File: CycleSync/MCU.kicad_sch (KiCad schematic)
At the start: 0 parts

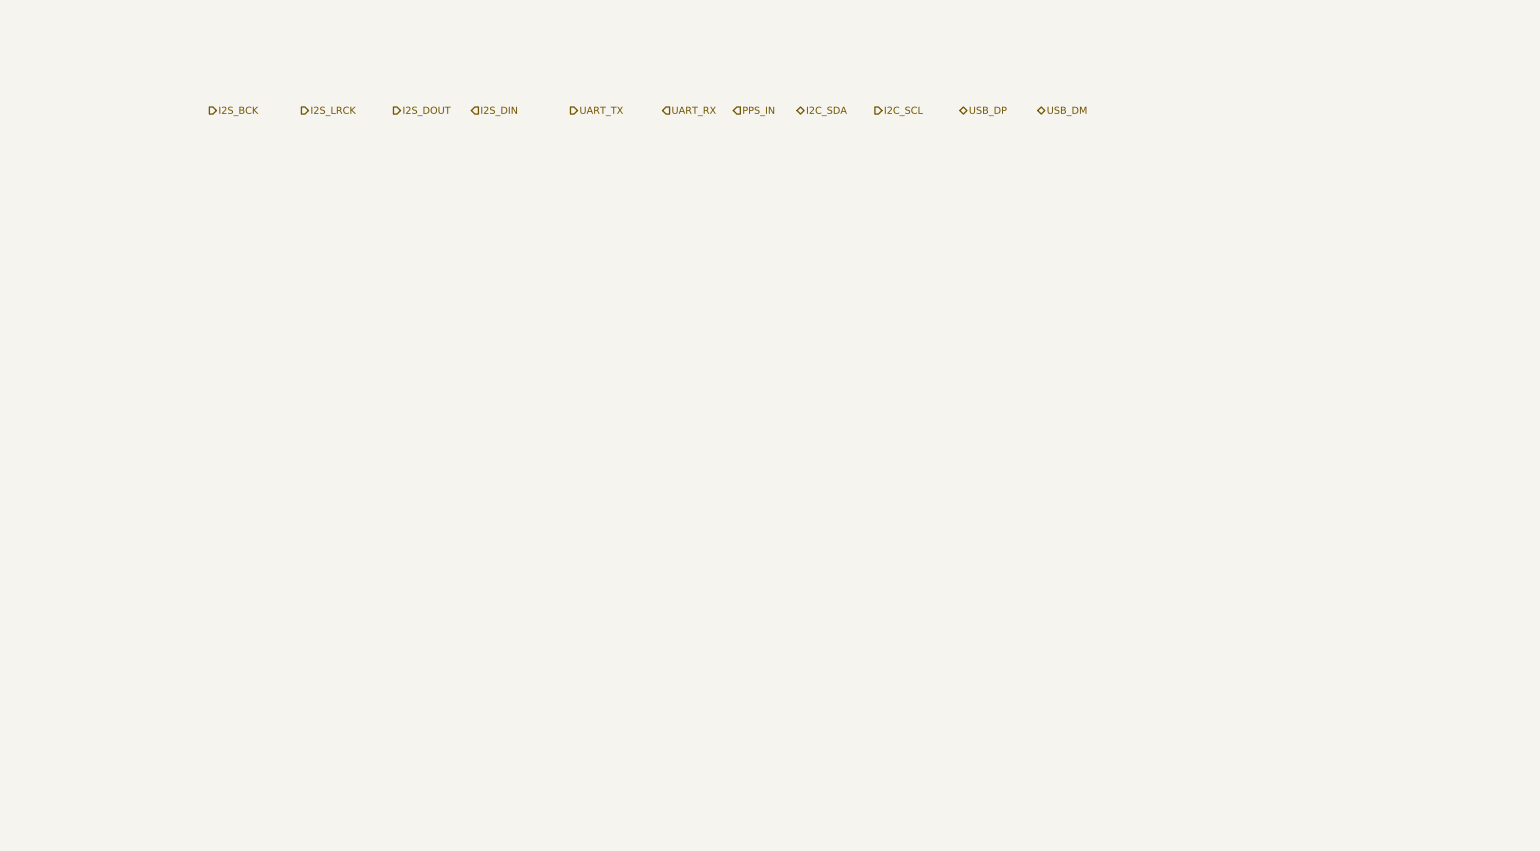
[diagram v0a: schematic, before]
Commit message: M1.2: MCU core supply, fixed-function pins, GPIO0-8 assignment
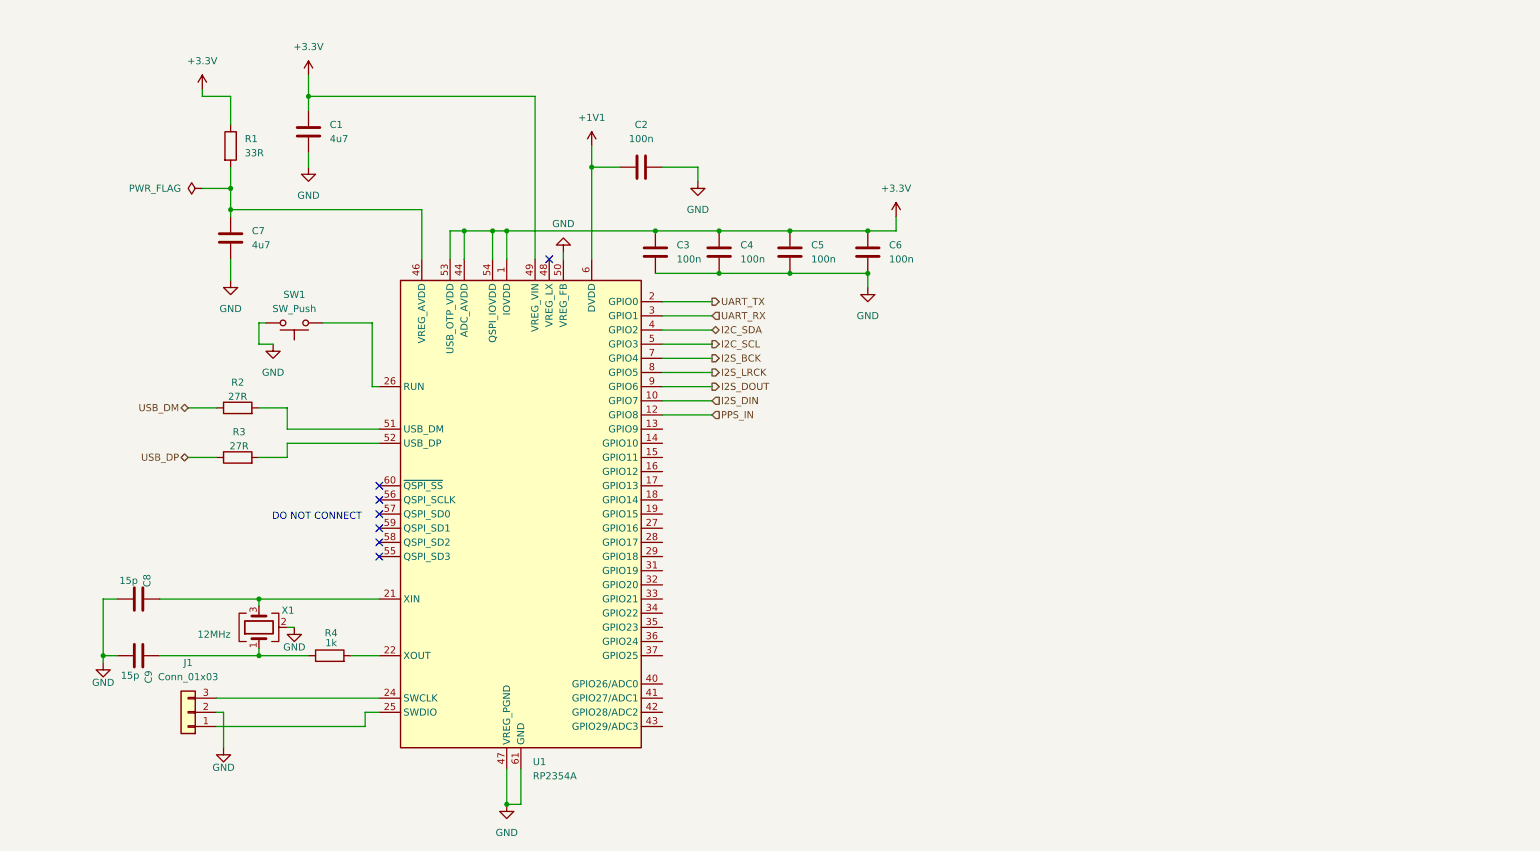
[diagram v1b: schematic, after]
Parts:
- added C1, C7: 4u7, symbol Device:C
- added C2, C3, C4, C5, C6: 100n, symbol Device:C
- added C8, C9: 15p, symbol Device:C
- added J1: Conn_01x03, symbol Connector_Generic:Conn_01x03
- added R1: 33R, symbol Device:R
- added R2, R3: 27R, symbol Device:R
- added R4: 1k, symbol Device:R
- added SW1: SW_Push, symbol Switch:SW_Push
- added U1: RP2354A, Package_DFN_QFN:QFN-60-1EP_7x7mm_P0.4mm_EP3.4x3.4mm, symbol MCU_RaspberryPi:RP2354A
- added X1: 12MHz, symbol Device:Crystal_GND24
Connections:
- net I2C_SCL: now also U1.5 (GPIO3)
- net I2C_SDA: now also U1.4 (GPIO2)
- net I2S_BCK: now also U1.7 (GPIO4)
- net I2S_DIN: now also U1.10 (GPIO7)
- net I2S_DOUT: now also U1.9 (GPIO6)
- net I2S_LRCK: now also U1.8 (GPIO5)
- net PPS_IN: now also U1.12 (GPIO8)
- net UART_RX: now also U1.3 (GPIO1)
- net UART_TX: now also U1.2 (GPIO0)
- net USB_DM: now also R2.1
- net USB_DP: now also R3.1
- new net: C9.2, R4.1, X1.1
- new net: C8.2, U1.21 (XIN), X1.3
- new net: J1.1 (Pin_1), U1.25 (SWDIO)
- new net: J1.3 (Pin_3), U1.24 (SWCLK)
- new net: R4.2, U1.22 (XOUT)
- new net: SW1.1, U1.26 (RUN)
- new net: C7.1, R1.2, U1.46 (VREG_AVDD)
- new net: R2.2, U1.51 (USB_DM)
- new net: R3.2, U1.52 (USB_DP)
- new net +1V1: C2.1, U1.23 (DVDD), U1.39 (DVDD), U1.6 (DVDD)
- new net +3.3V: C1.1, C3.2, C4.2, C5.2, C6.2, R1.1, U1.1 (IOVDD), U1.11 (IOVDD), U1.20 (IOVDD), U1.30 (IOVDD), U1.38 (IOVDD), U1.44 (ADC_AVDD), U1.45 (IOVDD), U1.49 (VREG_VIN), U1.53 (USB_OTP_VDD), U1.54 (QSPI_IOVDD)
- new net GND: C1.2, C2.2, C3.1, C4.1, C5.1, C6.1, C7.2, C8.1, C9.1, J1.2 (Pin_2), SW1.2, U1.47 (VREG_PGND), U1.50 (VREG_FB), U1.61 (GND), X1.2 (G), X1.4 (G)
- no-connect marks 0 -> 7
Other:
- note added: "DO NOT CONNECT"

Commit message: s
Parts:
- added C10, C11, C12, C5: 100n, symbol Device:C
- added C13: 10u, symbol Device:C
- added C4: 4.7u, symbol Device:C
- added R2, R3: 1K, symbol Device:R
- added R53, R54: 2k2, symbol Device:R
- added SW2: SW_Push, symbol Switch:SW_Push
- C1: renamed from C7; footprint (none) -> Capacitor_SMD:C_0402_1005Metric
- R1: footprint (none) -> Resistor_SMD:R_0402_1005Metric
- X1: value 12MHz -> Abracon ABM8-272-T3
- renumbered C8 to C14, C9 to C15, C1 to C2, C2 to C3, C3 to C6, C4 to C7, C5 to C8, C6 to C9, R2 to R4, R3 to R5, R4 to R6
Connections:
- net +1V1: now also C3.2, C4.2, C5.2; no longer C3.1
- net GND: now also C3.1, C10.1, C11.1, C12.1, C13.1, C4.1, C5.1, R2.1, SW2.2; no longer C3.2, SW1.2
- net I2C_SCL: now also R54.2
- net I2C_SDA: now also R53.2
- net XOUT_XTAL: now reaches C15.2, R6.1, X1.1
- net XIN: now reaches C14.2, U1.21 (XIN), X1.3
- net SWDIO: now reaches J1.1 (Pin_1), U1.25 (SWDIO)
- net SWCLK: now reaches J1.3 (Pin_3), U1.24 (SWCLK)
- net GNSS_FIX_STATUS: now reaches U1.13 (GPIO9)
- net GNSS_FIX_LED: now reaches U1.14 (GPIO10)
- net GNSS_RESET_N: now reaches U1.15 (GPIO11)
- net GNSS_BCKP_CUTOFF: now reaches U1.16 (GPIO12)
- net GNSS_VCC_CUTOFF: now reaches U1.17 (GPIO13)
- net PD_IRQ: now reaches U1.18 (GPIO14)
- net XOUT: now reaches R6.2, U1.22 (XOUT)
- net RUN: now reaches SW1.1, U1.26 (RUN)
- net VREG_AVDD: now reaches C1.1, R1.2, U1.46 (VREG_AVDD)
- net USB_MCU_N: now reaches R4.2, U1.51 (USB_DM)
- net USB_MCU_P: now reaches R5.2, U1.52 (USB_DP)
- net BOOTSEL: now reaches U1.60 (~{QSPI_SS})
- net BOOTSEL: now also R3.2
- net +3.3V renamed +3V3_DIG
- net +3V3_DIG: now also C10.2, C11.2, C12.2, C13.2, R53.1, R54.1
- net USB_DM renamed USB_D_N
- net USB_DP renamed USB_D_P
- new net BOOTSEL_SW: R3.1, SW2.1
- new net RUN_SW_GND: R2.2, SW1.2
- no-connect marks 7 -> 21
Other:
- note added: "+1V1 CORE DECOUPLING"
- note added: "+3V3_DIG I/O DECOUPLING"
- note added: "12 MHz CLOCK"
- note added: "FILTERED ANALOG SUPPLIES"
- note added: "GPIO15–GPIO29 RESERVED / UNUSED — NO CONNECT"
- note added: "NO-PD-OPTION I²C1 PULL-UPS R53/R54 = 2.2 kΩ TO +3V3_DIG POPULATE ONLY IN NO-PD BUILDS. PD BUILDS USE R37/R38 ON USB_PD SHEET. NEVER POPULATE BOTH PULL-UP PAIRS."
- note added: "QSPI_SCLK AND QSPI_SD0-SD3: INTERNAL FLASH DO NOT CONNECT EXTERNALLY"
- note added: "RUN / RESET"
- note added: "SIGNAL NAMES ARE FROM THE MCU PERSPECTIVE; UART_TX IS TRANSMITTED BY U1."
- note added: "SWD DEBUG HEADER"
- note added: "USB 2.0 FULL-SPEED"
- note removed: "DO NOT CONNECT"
- title: (none) -> RP2354A MCU CORE & INTERFACES
- moved on the sheet: C1, C14, C15, C2, C3, C6, C7, C8, C9, J1, R1, R4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

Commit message: verified schematic wirings
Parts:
- renumbered R4 to R3, R5 to R4, R3 to R5, R53 to R7, R54 to R8
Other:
- note added: "NO-PD-OPTION I²C1 PULL-UPS R7/R8 = 2.2 kΩ TO +3V3_DIG POPULATE ONLY IN NO-PD BUILDS. PD BUILDS USE R39/R40 ON USB_PD SHEET. NEVER POPULATE BOTH PULL-UP PAIRS."
- note removed: "NO-PD-OPTION I²C1 PULL-UPS R53/R54 = 2.2 kΩ TO +3V3_DIG POPULATE ONLY IN NO-PD BUILDS. PD BUILDS USE R37/R38 ON USB_PD SHEET. NEVER POPULATE BOTH PULL-UP PAIRS."
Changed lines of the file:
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@@
 		)
 	)
-	(text "NO-PD-OPTION I²C1 PULL-UPS\n\nR53/R54 = 2.2 kΩ TO +3V3_DIG\nPOPULATE ONLY IN NO-PD BUILDS.\n\nPD BUILDS USE R37/R38 ON USB_PD SHEET.\nNEVER POPULATE BOTH PULL-UP PAIRS."
+	(text "NO-PD-OPTION I²C1 PULL-UPS\n\nR7/R8 = 2.2 kΩ TO +3V3_DIG\nPOPULATE ONLY IN NO-PD BUILDS.\n\nPD BUILDS USE R39/R40 ON USB_PD SHEET.\nNEVER POPULATE BOTH PULL-UP PAIRS."
 		(exclude_from_sim no)
 		(at 264.16 157.48 0)
@@
 		(in_pos_files yes)
 		(dnp no)
-		(property "Reference" "R3"
+		(property "Reference" "R5"
 			(at 53.594 104.648 90)
 			(show_name no)
@@
 			(project "CycleSync"
 				(path "/3f2cc6af-e67b-48ad-b391-ff7619611bd8/3d349b1e-1bc7-4ddf-90e2-c9fab86974ff"
-					(reference "R3")
+					(reference "R5")
 					(unit 1)
 				)
@@
 		(in_pos_files yes)
 		(dnp no)
-		(property "Reference" "R54"
+		(property "Reference" "R8"
 			(at 216.154 92.456 0)
 			(show_name no)
@@
 			(project "CycleSync"
 				(path "/3f2cc6af-e67b-48ad-b391-ff7619611bd8/3d349b1e-1bc7-4ddf-90e2-c9fab86974ff"
-					(reference "R54")
+					(reference "R8")
 					(unit 1)
 				)
@@
 		(in_pos_files yes)
 		(dnp no)
-		(property "Reference" "R5"
+		(property "Reference" "R4"
 			(at 87.884 97.028 90)
 			(show_name no)
@@
 			(project "CycleSync"
 				(path "/3f2cc6af-e67b-48ad-b391-ff7619611bd8/3d349b1e-1bc7-4ddf-90e2-c9fab86974ff"
-					(reference "R5")
+					(reference "R4")
 					(unit 1)
 				)
@@
 		(in_pos_files yes)
 		(dnp no)
-		(property "Reference" "R53"
+		(property "Reference" "R7"
 			(at 200.914 93.218 0)
 			(show_name no)
@@
 			(project "CycleSync"
 				(path "/3f2cc6af-e67b-48ad-b391-ff7619611bd8/3d349b1e-1bc7-4ddf-90e2-c9fab86974ff"
-					(reference "R53")
+					(reference "R7")
 					(unit 1)
 				)
@@
 		(in_pos_files yes)
 		(dnp no)
-		(property "Reference" "R4"
+		(property "Reference" "R3"
 			(at 87.63 88.138 90)
 			(show_name no)
@@
 			(project "CycleSync"
 				(path "/3f2cc6af-e67b-48ad-b391-ff7619611bd8/3d349b1e-1bc7-4ddf-90e2-c9fab86974ff"
-					(reference "R4")
+					(reference "R3")
 					(unit 1)
 				)

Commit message: added some new testpoints for I2C
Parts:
- added TP1: I2C_SDA, TestPoint:TestPoint_Pad_D1.5mm, symbol Connector:TestPoint
- added TP2: I2C_SCL, TestPoint:TestPoint_Pad_D1.5mm, symbol Connector:TestPoint
- C1: footprint Capacitor_SMD:C_0402_1005Metric -> Capacitor_SMD:C_0805_2012Metric
- C10, C11, C12, C14, C15, C3, C5, C6, C7, C8, C9: footprint (none) -> Capacitor_SMD:C_0402_1005Metric
- C13, C2: footprint (none) -> Capacitor_SMD:C_0805_2012Metric
- C4: value 4.7u -> 4u7; footprint (none) -> Capacitor_SMD:C_0805_2012Metric
- R2, R3, R4, R5, R6, R7, R8: footprint (none) -> Resistor_SMD:R_0402_1005Metric
- X1: footprint (none) -> Crystal:Crystal_SMD_Abracon_ABM8G-4Pin_3.2x2.5mm
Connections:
- net I2C_SCL: now also TP2.1
- net I2C_SDA: now also TP1.1
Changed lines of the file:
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@@
 	(text "SIGNAL NAMES ARE FROM THE MCU PERSPECTIVE; UART_TX IS TRANSMITTED BY U1.\n"
 		(exclude_from_sim no)
-		(at 215.9 74.676 0)
+		(at 215.9 72.39 0)
 		(effects
 			(font
@@
 	)
 	(junction
+		(at 226.06 81.28)
+		(diameter 0)
+		(color 0 0 0 0)
+	)
+	(junction
 		(at 212.09 69.85)
 		(diameter 0)
@@
 	)
 	(junction
+		(at 195.58 78.74)
+		(diameter 0)
+		(color 0 0 0 0)
+	)
+	(junction
 		(at 187.96 46.99)
 		(diameter 0)
@@
 	(wire
 		(pts
+			(xy 195.58 78.74) (xy 205.74 78.74)
+		)
+		(stroke
+			(width 0)
+			(type default)
+		)
+	)
+	(wire
+		(pts
 			(xy 120.65 57.15) (xy 86.36 57.15)
 		)
@@
 	(wire
 		(pts
-			(xy 163.83 78.74) (xy 205.74 78.74)
+			(xy 163.83 78.74) (xy 195.58 78.74)
 		)
 		(stroke
@@
 	(wire
 		(pts
+			(xy 226.06 81.28) (xy 234.95 81.28)
+		)
+		(stroke
+			(width 0)
+			(type default)
+		)
+	)
+	(wire
+		(pts
 			(xy 224.79 69.85) (xy 238.76 69.85)
 		)
@@
 	(wire
 		(pts
-			(xy 220.98 81.28) (xy 234.95 81.28)
+			(xy 220.98 81.28) (xy 226.06 81.28)
 		)
 		(stroke
@@
 			)
 		)
-		(property "Footprint" ""
+		(property "Footprint" "Capacitor_SMD:C_0402_1005Metric"
 			(at 164.1348 60.96 0)
 			(hide yes)
@@
 			)
 		)
-		(property "Footprint" ""
+		(property "Footprint" "Crystal:Crystal_SMD_Abracon_ABM8G-4Pin_3.2x2.5mm"
 			(at 66.04 132.08 0)
 			(hide yes)
@@
 			)
 		)
-		(property "Footprint" ""
+		(property "Footprint" "Resistor_SMD:R_0402_1005Metric"
 			(at 53.34 110.998 90)
 			(hide yes)
@@
 			)
 		)
-		(property "Footprint" ""
+		(property "Footprint" "Capacitor_SMD:C_0402_1005Metric"
 			(at 57.15 126.0348 0)
 			(hide yes)
@@
 			)
 		)
-		(property "Footprint" ""
+		(property "Footprint" "Resistor_SMD:R_0402_1005Metric"
 			(at 74.93 79.248 90)
 			(hide yes)
@@
 			)
 		)
-		(property "Footprint" ""
+		(property "Footprint" "Resistor_SMD:R_0402_1005Metric"
 			(at 222.758 93.98 90)
 			(hide yes)
@@
 			)
 		)
-		(property "Footprint" ""
+		(property "Footprint" "Capacitor_SMD:C_0402_1005Metric"
 			(at 175.5648 60.96 0)
 			(hide yes)
@@
 	)
 	(symbol
+		(lib_id "Connector:TestPoint")
+		(at 226.06 81.28 0)
+		(unit 1)
+		(body_style 1)
+		(exclude_from_sim no)
+		(in_bom yes)
+		(on_board yes)
+		(in_pos_files yes)
+		(dnp no)
+		(fields_autoplaced yes)
+		(property "Reference" "TP2"
+			(at 228.6 76.7079 0)
+			(show_name no)
+			(do_not_autoplace no)
+			(effects
+				(font
+					(size 1.27 1.27)
+				)
+				(justify left)
+			)
+		)
+		(property "Value" "I2C_SCL"
+			(at 228.6 79.2479 0)
+			(show_name no)
+			(do_not_autoplace no)
+			(effects
+				(font
+					(size 1.27 1.27)
+				)
+				(justify left)
+			)
+		)
+		(property "Footprint" "TestPoint:TestPoint_Pad_D1.5mm"
+			(at 231.14 81.28 0)
+			(hide yes)
+			(show_name no)
+			(do_not_autoplace no)
+			(effects
+				(font
+					(size 1.27 1.27)
+				)
+			)
+		)
+		(property "Datasheet" ""
+			(at 231.14 81.28 0)
+			(hide yes)
+			(show_name no)
+			(do_not_autoplace no)
+			(effects
+				(font
+					(size 1.27 1.27)
+				)
+			)
+		)
+		(property "Description" "test point"
+			(at 226.06 81.28 0)
+			(hide yes)
+			(show_name no)
+			(do_not_autoplace no)
+			(effects
+				(font
+					(size 1.27 1.27)
+				)
+			)
+		)
+		(pin "1"
+		)
+		(instances
+			(project "CycleSync"
+				(path "/3f2cc6af-e67b-48ad-b391-ff7619611bd8/3d349b1e-1bc7-4ddf-90e2-c9fab86974ff"
+					(reference "TP2")
+					(unit 1)
+				)
+			)
+		)
+	)
+	(symbol
 		(lib_id "power:GND")
 		(at 16.51 100.33 0)
@@
 	)
 	(symbol
+		(lib_id "Connector:TestPoint")
+		(at 195.58 78.74 0)
+		(unit 1)
+		(body_style 1)
+		(exclude_from_sim no)
+		(in_bom yes)
+		(on_board yes)
+		(in_pos_files yes)
+		(dnp no)
+		(fields_autoplaced yes)
+		(property "Reference" "TP1"
+			(at 198.12 74.1679 0)
+			(show_name no)
+			(do_not_autoplace no)
+			(effects
+				(font
+					(size 1.27 1.27)
+				)
+				(justify left)
+			)
+		)
+		(property "Value" "I2C_SDA"
+			(at 198.12 76.7079 0)
+			(show_name no)
+			(do_not_autoplace no)
+			(effects
+				(font
+					(size 1.27 1.27)
+				)
+				(justify left)
+			)
+		)
+		(property "Footprint" "TestPoint:TestPoint_Pad_D1.5mm"
+			(at 200.66 78.74 0)
+			(hide yes)
+			(show_name no)
+			(do_not_autoplace no)
+			(effects
+				(font
+					(size 1.27 1.27)
+				)
+			)
+		)
+		(property "Datasheet" ""
+			(at 200.66 78.74 0)
+			(hide yes)
+			(show_name no)
+			(do_not_autoplace no)
+			(effects
+				(font
+					(size 1.27 1.27)
+				)
+			)
+		)
+		(property "Description" "test point"
+			(at 195.58 78.74 0)
+			(hide yes)
+			(show_name no)
+			(do_not_autoplace no)
+			(effects
+				(font
+					(size 1.27 1.27)
+				)
+			)
+		)
+		(pin "1"
+		)
+		(instances
+			(project "CycleSync"
+				(path "/3f2cc6af-e67b-48ad-b391-ff7619611bd8/3d349b1e-1bc7-4ddf-90e2-c9fab86974ff"
+					(reference "TP1")
+					(unit 1)
+				)
+			)
+		)
+	)
+	(symbol
 		(lib_id "power:GND")
 		(at 187.96 49.53 0)
@@
 			)
 		)
-		(property "Footprint" ""
+		(property "Footprint" "Capacitor_SMD:C_0402_1005Metric"
 			(at 186.9948 39.37 0)
 			(hide yes)
@@
 			)
 		)
-		(property "Footprint" ""
+		(property "Footprint" "Resistor_SMD:R_0402_1005Metric"
 			(at 87.63 103.378 90)
 			(hide yes)
@@
 			)
 		)
-		(property "Footprint" ""
+		(property "Footprint" "Capacitor_SMD:C_0402_1005Metric"
 			(at 186.9948 60.96 0)
 			(hide yes)
@@
 			)
 		)
-		(property "Footprint" ""
+		(property "Footprint" "Capacitor_SMD:C_0805_2012Metric"
 			(at 251.7648 60.96 0)
 			(hide yes)
@@
 			)
 		)
-		(property "Footprint" ""
+		(property "Footprint" "Capacitor_SMD:C_0402_1005Metric"
 			(at 59.69 136.1948 0)
 			(hide yes)
@@
 			)
 		)
-		(property "Footprint" ""
+		(property "Footprint" "Capacitor_SMD:C_0402_1005Metric"
 			(at 211.1248 60.96 0)
 			(hide yes)
@@
 			)
 		)
-		(property "Footprint" ""
+		(property "Footprint" "Capacitor_SMD:C_0402_1005Metric"
 			(at 223.8248 60.96 0)
 			(hide yes)
@@
 			)
 		)
-		(property "Footprint" ""
+		(property "Footprint" "Capacitor_SMD:C_0805_2012Metric"
 			(at 101.2952 46.99 0)
 			(hide yes)
@@
 			)
 		)
-		(property "Footprint" ""
+		(property "Footprint" "Resistor_SMD:R_0402_1005Metric"
 			(at 207.518 93.98 90)
 			(hide yes)
@@
 			)
 		)
-		(property "Value" "4.7u"
+		(property "Value" "4u7"
 			(at 177.8 44.4499 0)
 			(show_name no)
@@
 			)
 		)
-		(property "Footprint" ""
+		(property "Footprint" "Capacitor_SMD:C_0805_2012Metric"
 			(at 173.0248 39.37 0)
 			(hide yes)
@@
 			)
 		)
-		(property "Footprint" ""
+		(property "Footprint" "Resistor_SMD:R_0402_1005Metric"
 			(at 87.63 94.488 90)
 			(hide yes)
@@
 			)
 		)
-		(property "Footprint" ""
+		(property "Footprint" "Capacitor_SMD:C_0402_1005Metric"
 			(at 159.0548 39.37 0)
 			(hide yes)
@@
 			)
 		)
-		(property "Footprint" "Capacitor_SMD:C_0402_1005Metric"
+		(property "Footprint" "Capacitor_SMD:C_0805_2012Metric"
 			(at 87.3252 66.04 0)
 			(hide yes)
@@
 			)
 		)
-		(property "Footprint" ""
+		(property "Footprint" "Capacitor_SMD:C_0402_1005Metric"
 			(at 199.6948 60.96 0)
 			(hide yes)
@@
 			)
 		)
-		(property "Footprint" ""
+		(property "Footprint" "Resistor_SMD:R_0402_1005Metric"
 			(at 90.17 138.938 90)
 			(hide yes)
@@
 			)
 		)
-		(property "Footprint" ""
+		(property "Footprint" "Capacitor_SMD:C_0402_1005Metric"
 			(at 237.7948 60.96 0)
 			(hide yes)

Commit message: added footprints and manufacturer part number
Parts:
- added TP29: GND_MCU, TestPoint:TestPoint_Pad_D1.5mm, symbol Connector:TestPoint
- C1, C2, C4: Distributor Link (none) -> https://jlcpcb.com/partdetail/2131-CL21A475KAQNNNE/C1779; MANUFACTURER (none) -> Samsung Electro-Mechanics; MPN (none) -> CL21A475KAQNNNE
- C10, C11, C12, C3, C5, C6, C7, C8, C9: Distributor Link (none) -> https://jlcpcb.com/partdetail/MurataElectronics-GRM155R71A1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; MANUFACTURER (none) -> Murata Electronics; MPN (none) -> GRM155R71A104KA01D
- C13: Distributor Link (none) -> https://jlcpcb.com/partdetail/236937-GRM21BZ71E106KE15L/C23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; MANUFACTURER (none) -> Murata Electronics; MPN (none) -> GRM21BZ71E106KE15L
- C14, C15: Distributor Link (none) -> https://jlcpcb.com/partdetail/MurataElectronics-GRM1555C1H1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; MANUFACTURER (none) -> Murata Electronics; MPN (none) -> GRM1555C1H150JA01D
- J1: footprint (none) -> Connector_JST:JST_SH_SM03B-SRSS-TB_1x03-1MP_P1.00mm_Horizontal; Distributor Link (none) -> https://jlcpcb.com/partdetail/JST-SM03B_SRSS_TB_LF_SN/C1604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; MANUFACTURER (none) -> JST; MPN (none) -> SM03B-SRSS-TB(LF)(SN)
- R1: Distributor Link (none) -> https://jlcpcb.com/partdetail/LIZElec-CR0402FF33R0G/C100382; MANUFACTURER (none) -> LIZ Elec; MPN (none) -> CR0402FF33R0G
- R2, R5, R6: Distributor Link (none) -> https://jlcpcb.com/partdetail/VishayIntertech-CRCW04021K00F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; MANUFACTURER (none) -> Vishay Intertech; MPN (none) -> CRCW04021K00FKED
- R3, R4: Distributor Link (none) -> https://jlcpcb.com/partdetail/25899-0402WGJ0270TCE/C25156; MANUFACTURER (none) -> UNI-ROYAL(Uniroyal Elec); MPN (none) -> 0402WGJ0270TCE
- R7, R8: Distributor Link (none) -> https://jlcpcb.com/partdetail/26622-0402WGF2201TCE/C25879; MANUFACTURER (none) -> UNI-ROYAL(Uniroyal Elec); MPN (none) -> 0402WGF2201TCE; now not fitted
- SW1, SW2: footprint (none) -> TS-1187A-B-A-B:SW_TS-1187A-B-A-B; Distributor Link (none) -> https://jlcpcb.com/partdetail/XKBConnection-TS_1187A_B_AB/C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; MANUFACTURER (none) -> XKB Connection; MPN (none) -> TS-1187A-B-A-B
- TP1, TP2: now left out of the parts list
- U1: Distributor Link (none) -> https://jlcpcb.com/partdetail/RaspberryPi-RP2354A/C41378174; MANUFACTURER (none) -> Raspberry Pi; MPN (none) -> RP2354A
- X1: footprint Crystal:Crystal_SMD_Abracon_ABM8G-4Pin_3.2x2.5mm -> ABM8-272-T3:XTAL_ABM8-272-T3; Distributor Link (none) -> https://jlcpcb.com/partdetail/AbraconLLC-ABM8_272T3/C206257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; MANUFACTURER (none) -> Abracon LLC; MPN (none) -> ABM8-272-T3
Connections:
- net GND: now also TP29.1
